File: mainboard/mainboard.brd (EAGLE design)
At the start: 158.8 x 159.4 mm, 60 parts, among them T1 NPN_BC817,215, T2 NPN_BC817,215, T3 NPN_BC817,215

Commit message: Mainboard rev1 wip
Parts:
- removed BOOST_EN: CONNEC_1X01, rhoban:CONNEC_1X01
- removed POWERCAP1, POWERCAP2, SOLENOID1, SOLENOID2: CONNEC_1X02BIG, rhoban:CONNEC_1X02_BIG
- removed R31, R9: 1K, rhoban:R0805
- removed R32, R33, R36: 3K, rhoban:R0805
- removed R34: 2M, rhoban:R0805
- removed R35: 10K, rhoban:R0805
- removed T1, T3, U$15: NPN_BC817,215, rhoban:SOT-23
- removed XT1: CONNEC_ALIM, rhoban:XT60
- added C2: 1uF, SparkFun-Passives:0805@1
- added REG3.3V1: REG_5V, rhoban:TRACOPOWER
- added U$10: DRV5023FAEDBZRQ1, rhoban:SOT-23
- added U$6: 47uF, rhoban:PANASONIC_D
- added U$7, U$8, U$9: (no value), rhoban:PANASONIC_D8
- added X1: JST-XH-06-PIN-LONG-PAD, Rembrandt Electronics - JST XH Connectors v1-0:JST-XH-06-PACKAGE-LONG-PAD
- R1: value 1K -> 10K
- R2, R3: value 3K -> 10K
- U$1, U$11: value TO-247A -> DRV5023FAEDBZRQ1; device to-247_n-channel_igbt:TO-247 -> rhoban:SOT-23
- U$5: value BOOSTER -> DRV5023FAEDBZRQ1; device rhoban:BOOSTER_390V -> rhoban:SOT-23
- moved R7 94.5 mm to (-35.3, -40.5), flipped to the bottom
- moved DRIVER4 90.6 mm to (-11.6, -50.1), turned to 0 degrees
- moved XT60 89.0 mm to (-37.4, 26.2), turned to 180 degrees
- moved U$5 78.3 mm to (14.5, -37.3), flipped to the bottom
- moved U$1 76.3 mm to (39.5, -37.3), flipped to the bottom, turned to 0 degrees
- moved U$11 66.9 mm to (-35.5, -37.3), flipped to the bottom, turned to 0 degrees
- moved DRIVER2 66.0 mm to (31.2, 43.5), turned to 180 degrees
- moved D3 65.0 mm to (3.03, -47.2), turned to 90 degrees
- moved R1 64.6 mm to (39.5, -40.5), flipped to the bottom, turned to 180 degrees
- moved R2 61.7 mm to (14.6, -40.7), flipped to the bottom, turned to 180 degrees
- moved R3 60.1 mm to (-10.4, -40.6), flipped to the bottom, turned to 180 degrees
- moved DRIVER3 59.5 mm to (-44.5, -50.1), turned to 0 degrees
- moved D2 49.6 mm to (-29.7, -47.2), turned to 90 degrees
- moved D1 48.4 mm to (16.6, 40.4), turned to 270 degrees
- moved U$2 41.4 mm to (71.5, -31.8), turned to 90 degrees
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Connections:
- net BAT2 renamed BAT
- removed net BAT1: MAPLE.X8, R7.1, R9.2
- removed net N$1: R1.2, T1.1
- removed net N$17: R31.2, T3.1
- removed net N$2: SOLENOID1.P$2, U$1.P$2
- removed net N$35: R33.1, T3.3, U$11.P$1
- removed net N$36: SOLENOID2.P$2, U$11.P$2
- removed net N$37: BOOST_EN.1, U$15.3
- removed net N$38: R36.1, U$15.1
- removed net N$4: R3.1, T1.3, U$1.P$1
- removed net VBOOST: POWERCAP1.P$2, POWERCAP2.P$2, R34.2, SOLENOID1.P$1, SOLENOID2.P$1, U$5.OUT+
- removed net VMID: D1.2, D2.2, D3.2, D4.2, D5.2, R7.2, XT1.GND, XT60.V+
- new net 12V: C2.2, D1.2, D2.2, D3.2, D4.2, D5.2, REG3.3V1.P$3, U$6.+
- new net HALL1: MAPLE.X14, R1.1, U$1.2
- new net HALL2: MAPLE.X8, R2.1, U$5.2
- new net HALL3: MAPLE.X2, R3.1, U$10.2
- new net HALL4: MAPLE.X31, R7.1, U$11.2
- net 3.3: now also R1.2, R3.2, R7.2, U$1.1, U$10.1, U$11.1, U$5.1, U$7.+, U$8.+, U$9.+; no longer R32.2
- net BOOST_EN: now also X1.3; no longer R36.2
- net CAP: now also X1.6; no longer R34.1, R35.2
- net GND: now also C2.1, REG3.3V1.P$2, U$1.3, U$10.3, U$11.3, U$5.3, U$6.-, U$7.-, U$8.-, U$9.-, X1.1; no longer POWERCAP1.P$1, POWERCAP2.P$1, R35.1, R9.1, T1.2, T3.2, U$1.P$3, U$11.P$3, U$15.2, U$5.IN-, U$5.OUT-
- net KICK1: now also X1.4; no longer R1.1, R2.1
- net KICK2: now also X1.5; no longer R31.1, R32.1
- net VIN: now also REG3.3V1.P$1, X1.2, XT60.V+; no longer R3.2, R33.2, U$5.VIN, XT1.V+
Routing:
- net GND: track 89.1 -> 0.00 mm
- net VBOOST: track 26.0 -> 0.00 mm
- net N$2: track 13.5 -> 0.00 mm
- net N$36: track 11.6 -> 0.00 mm
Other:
- board size 158.8 x 159.4 mm -> 158.8 x 136.4 mm
- board text added: "12V"
- board text added: "3.3V"
- board text added: "5V"
- board text added: "RHOBAN SSL rev1"
- board text removed: "BOOST_EN"
- board text removed: "REV0"
- board text removed: "RHOBAN SSL MAINBOARD"
- board text removed: "RHOBAN SSL rev0"

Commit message: Updating designs
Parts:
- moved D1 1.24 mm to (15.4, 40.7)
- moved D5 1.20 mm to (36.5, -47.1)
- moved D4 1.17 mm to (-17.0, 40.7)
- moved D3 1.10 mm to (4.13, -47.2)
- moved D2 0.91 mm to (-28.8, -47.3)
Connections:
- net DRIVERS_CS2: now also MAPLE.X1; no longer MAPLE.X26
- net IRQ3: now also MAPLE.X0; no longer MAPLE.X25
- net KICK1: now also MAPLE.X25; no longer MAPLE.X0
- net KICK2: now also MAPLE.X26; no longer MAPLE.X1
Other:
- board text added: "DRIVER"
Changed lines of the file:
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@@
 <dimension x1="-59.75" y1="43.75" x2="-59.75" y2="-38.25" x3="-107.75" y3="2.75" layer="51"/>
 <dimension x1="1.7" y1="60.8" x2="2" y2="-77.5" x3="113.45066875" y3="-8.107915625" layer="51"/>
-<text x="38.75" y="-9.5" size="10" layer="112" rot="R180">1</text>
-<text x="8" y="-8.75" size="10" layer="112" rot="R180">2</text>
-<text x="-12.25" y="13.25" size="10" layer="112" rot="R180">5</text>
-<text x="-25" y="-8.5" size="10" layer="112" rot="R180">3</text>
-<text x="19.5" y="12.75" size="10" layer="112" rot="R180">4</text>
+<text x="37.25" y="-21.7" size="10" layer="112" rot="R180">1</text>
+<text x="6.5" y="-21.85" size="10" layer="112" rot="R180">2</text>
+<text x="-12.25" y="24.65" size="10" layer="112" rot="R180">5</text>
+<text x="-26.2" y="-21.2" size="10" layer="112" rot="R180">3</text>
+<text x="19.5" y="24.15" size="10" layer="112" rot="R180">4</text>
 <text x="-55.25" y="-14" size="1.778" layer="121">3.3V</text>
 <text x="-54.5" y="-23.5" size="1.778" layer="121">5V</text>
@@
 <wire x1="12.431" y1="-66.38" x2="12.744" y2="-66.525" width="0" layer="20"/>
 <wire x1="12.744" y1="-66.525" x2="13.029" y2="-66.725" width="0" layer="20"/>
+<text x="38.7" y="-34" size="3" layer="122">1</text>
+<text x="13.3" y="-34.5" size="3" layer="122">2</text>
+<text x="-11.6" y="-34.2" size="3" layer="122">3</text>
+<text x="-36.7" y="-34.5" size="3" layer="122">4</text>
+<text x="-38.5" y="-20.6" size="3" layer="121">DRIVER</text>
+<text x="-5.4" y="-20.8" size="3" layer="121">DRIVER</text>
+<text x="25.6" y="-20.9" size="3" layer="121">DRIVER</text>
+<text x="8.4" y="24.8" size="3" layer="121">DRIVER</text>
+<text x="-23.9" y="25" size="3" layer="121">DRIVER</text>
 </plain>
 <attributes>
@@
 <attribute name="FARNELL" value="1593459,1593459,1593463" x="-1.285" y="43.515" size="1.778" layer="27" rot="R180" display="off"/>
 </element>
-<element name="D5" library="SparkFun-DiscreteSemi" package="SOD-323" value="" x="35.265" y="-47.11" rot="R90">
-<attribute name="FARNELL" value="8737843RL" x="31.455" y="-50.92" size="1.778" layer="27" rot="R90" display="off"/>
-</element>
-<element name="D1" library="SparkFun-DiscreteSemi" package="SOD-323" value="" x="16.62" y="40.36" rot="R270">
-<attribute name="FARNELL" value="8737843RL" x="16.62" y="40.36" size="1.778" layer="27" rot="R270" display="off"/>
-</element>
-<element name="D2" library="SparkFun-DiscreteSemi" package="SOD-323" value="" x="-29.67" y="-47.155" rot="R90">
-<attribute name="FARNELL" value="8737843RL" x="-29.67" y="-47.155" size="1.778" layer="27" rot="R90" display="off"/>
-</element>
-<element name="D3" library="SparkFun-DiscreteSemi" package="SOD-323" value="" x="3.03" y="-47.155" rot="R90">
-<attribute name="FARNELL" value="8737843RL" x="3.03" y="-47.155" size="1.778" layer="27" rot="R90" display="off"/>
-</element>
-<element name="D4" library="SparkFun-DiscreteSemi" package="SOD-323" value="" x="-15.89" y="40.34" rot="R270">
-<attribute name="FARNELL" value="8737843RL" x="-15.89" y="40.34" size="1.778" layer="27" rot="R270" display="off"/>
+<element name="D5" library="SparkFun-DiscreteSemi" package="SOD-323" value="" x="36.465" y="-47.11" rot="R90">
+<attribute name="FARNELL" value="8737843RL" x="32.655" y="-50.92" size="1.778" layer="27" rot="R90" display="off"/>
+</element>
+<element name="D1" library="SparkFun-DiscreteSemi" package="SOD-323" value="" x="15.42" y="40.66" rot="R270">
+<attribute name="FARNELL" value="8737843RL" x="15.42" y="40.66" size="1.778" layer="27" rot="R270" display="off"/>
+</element>
+<element name="D2" library="SparkFun-DiscreteSemi" package="SOD-323" value="" x="-28.77" y="-47.255" rot="R90">
+<attribute name="FARNELL" value="8737843RL" x="-28.77" y="-47.255" size="1.778" layer="27" rot="R90" display="off"/>
+</element>
+<element name="D3" library="SparkFun-DiscreteSemi" package="SOD-323" value="" x="4.13" y="-47.155" rot="R90">
+<attribute name="FARNELL" value="8737843RL" x="4.13" y="-47.155" size="1.778" layer="27" rot="R90" display="off"/>
+</element>
+<element name="D4" library="SparkFun-DiscreteSemi" package="SOD-323" value="" x="-16.99" y="40.74" rot="R270">
+<attribute name="FARNELL" value="8737843RL" x="-16.99" y="40.74" size="1.778" layer="27" rot="R270" display="off"/>
 </element>
 <element name="R10" library="rhoban" package="R0805" value="10K" x="34.635" y="32.3" rot="R180">
@@
 <signals>
 <signal name="KICK2">
-<contactref element="MAPLE" pad="X1"/>
 <contactref element="X1" pad="5"/>
-<wire x1="-1.56" y1="55.25" x2="57.37" y2="10.2" width="0" layer="19" extent="1-1"/>
+<contactref element="MAPLE" pad="X26"/>
+<wire x1="-1.56" y1="55.25" x2="42.13" y2="17.82" width="0" layer="19" extent="1-1"/>
 </signal>
 <signal name="3.3" class="1">
@@
 </signal>
 <signal name="IRQ3">
-<contactref element="MAPLE" pad="X25"/>
 <contactref element="COM3" pad="IRQ"/>
-<wire x1="6.985" y1="-60.325" x2="42.13" y2="20.36" width="0" layer="19" extent="1-1"/>
+<contactref element="MAPLE" pad="X0"/>
+<wire x1="6.985" y1="-60.325" x2="57.37" y2="7.66" width="0" layer="19" extent="1-1"/>
 </signal>
 <signal name="IRQ2">
@@
 </signal>
 <signal name="KICK1">
-<contactref element="MAPLE" pad="X0"/>
 <contactref element="X1" pad="4"/>
-<wire x1="0.98" y1="55.25" x2="57.37" y2="7.66" width="0" layer="19" extent="1-1"/>
+<contactref element="MAPLE" pad="X25"/>
+<wire x1="0.98" y1="55.25" x2="42.13" y2="20.36" width="0" layer="19" extent="1-1"/>
 </signal>
 <signal name="BOOST_EN">
@@
 </signal>
 <signal name="DRIVERS_CS2">
-<contactref element="MAPLE" pad="X26"/>
 <contactref element="DRIVER2" pad="CS"/>
-<wire x1="42.13" y1="17.82" x2="19.0578" y2="44.0478" width="0" layer="19" extent="1-1"/>
+<contactref element="MAPLE" pad="X1"/>
+<wire x1="19.0578" y1="44.0478" x2="57.37" y2="10.2" width="0" layer="19" extent="1-1"/>
 </signal>
 <signal name="DRIVERS_CS1">
@@
 <contactref element="DRIVER1" pad="VDRIVER"/>
 <contactref element="D5" pad="1"/>
-<wire x1="35.265" y1="-48.26" x2="35.3672" y2="-50.7978" width="0" layer="19" extent="1-1"/>
+<wire x1="36.465" y1="-48.26" x2="35.3672" y2="-50.7978" width="0" layer="19" extent="1-1"/>
 </signal>
 <signal name="N$9">
 <contactref element="DRIVER4" pad="VDRIVER"/>
 <contactref element="D3" pad="1"/>
-<wire x1="3.03" y1="-48.305" x2="3.1322" y2="-50.5928" width="0" layer="19" extent="1-1"/>
+<wire x1="4.13" y1="-48.305" x2="3.1322" y2="-50.5928" width="0" layer="19" extent="1-1"/>
 </signal>
 <signal name="N$10">
 <contactref element="DRIVER5" pad="VDRIVER"/>
 <contactref element="D4" pad="1"/>
-<wire x1="-15.89" y1="41.49" x2="-15.9922" y2="44.0278" width="0" layer="19" extent="1-1"/>
+<wire x1="-16.99" y1="41.89" x2="-15.9922" y2="44.0278" width="0" layer="19" extent="1-1"/>
 </signal>
 <signal name="N$12">
 <contactref element="DRIVER3" pad="VDRIVER"/>
 <contactref element="D2" pad="1"/>
-<wire x1="-29.67" y1="-48.305" x2="-29.8178" y2="-50.5928" width="0" layer="19" extent="1-1"/>
+<wire x1="-28.77" y1="-48.405" x2="-29.8178" y2="-50.5928" width="0" layer="19" extent="1-1"/>
 </signal>
 <signal name="N$13">
 <contactref element="DRIVER2" pad="VDRIVER"/>
 <contactref element="D1" pad="1"/>
-<wire x1="16.62" y1="41.51" x2="16.5178" y2="44.0478" width="0" layer="19" extent="1-1"/>
+<wire x1="15.42" y1="41.81" x2="16.5178" y2="44.0478" width="0" layer="19" extent="1-1"/>
 </signal>
 <signal name="COM_CE">
@@
 <wire x1="-61.35" y1="-27.5" x2="-69.25" y2="-24.1" width="0" layer="19" extent="1-1"/>
 <wire x1="-55.33" y1="-27.75" x2="-61.35" y2="-27.5" width="0" layer="19" extent="1-1"/>
-<wire x1="-29.67" y1="-46.005" x2="-55.33" y2="-27.75" width="0" layer="19" extent="1-1"/>
-<wire x1="3.03" y1="-46.005" x2="-29.67" y2="-46.005" width="0" layer="19" extent="1-1"/>
-<wire x1="35.265" y1="-45.96" x2="3.03" y2="-46.005" width="0" layer="19" extent="1-1"/>
-<wire x1="-15.89" y1="39.19" x2="-55.33" y2="-27.75" width="0" layer="19" extent="1-1"/>
-<wire x1="16.62" y1="39.21" x2="-15.89" y2="39.19" width="0" layer="19" extent="1-1"/>
+<wire x1="-28.77" y1="-46.105" x2="-55.33" y2="-27.75" width="0" layer="19" extent="1-1"/>
+<wire x1="4.13" y1="-46.005" x2="-28.77" y2="-46.105" width="0" layer="19" extent="1-1"/>
+<wire x1="36.465" y1="-45.96" x2="4.13" y2="-46.005" width="0" layer="19" extent="1-1"/>
+<wire x1="-16.99" y1="39.59" x2="-55.33" y2="-27.75" width="0" layer="19" extent="1-1"/>
+<wire x1="15.42" y1="39.51" x2="-16.99" y2="39.59" width="0" layer="19" extent="1-1"/>
 </signal>
 <signal name="BAT">

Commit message: mainboard updates
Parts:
- added U$15: SRB22A2FBBNN, rhoban:SRB22A2FBBNN
- moved R11 110.5 mm to (-50.5, -40.7)
- moved R10 110.3 mm to (-50.5, -37.9)
- moved RECEIVE 21.2 mm to (-26.5, 56.1)
- moved R6 21.2 mm to (-25.9, 52.3)
- moved U$8 9.24 mm to (65.6, -10.1), turned to 0 degrees
- moved U$9 8.10 mm to (-10.1, -60.9), turned to 270 degrees
- moved XT60 5.89 mm to (-38.4, 20.4)
- moved U$7 5.32 mm to (-63.0, 17.3), turned to 180 degrees
- moved C2 1.02 mm to (-69.0, -24.0)
- moved R8 0.71 mm to (63.4, 32.8), turned to 180 degrees
- moved C7 0.60 mm to (-69.4, -9.59)
- moved C1 0.32 mm to (-69.2, -16.7)
- moved U$13 0.25 mm to (68.8, 22.9), turned to 270 degrees
- moved D1 0.14 mm to (15.5, 40.6)
- moved DRIVER2 0.08 mm to (31.3, 43.5)
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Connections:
- new net VIN_BAT: U$15.P$2, XT60.V+
- net VIN: now also U$15.P$1; no longer XT60.V+
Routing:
- net VIN: track 0.00 -> 172.7 mm
- net GND: track 0.00 -> 161.0 mm
- net VIN_BAT: track 0.00 -> 19.4 mm
- net 3.3: track 0.00 -> 4.44 mm, vias 0 -> 1
- net N$7: track 0.00 -> 4.40 mm, vias 0 -> 1
- net N$13: track 0.00 -> 2.75 mm
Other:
- board text added: "COM1"
- board text added: "COM2"
- board text added: "COM3"
- board text added: "IR EMIT"
- board text added: "IR RCV"
- board text added: "KICKER"
- board text added: "MAIN"
- board text added: "SWITCH"

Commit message: farnell attrs
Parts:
- moved U$12 78.9 mm to (-7.55, 54.8), turned to 0 degrees
- moved U$13 74.5 mm to (0.86, 53.5), turned to 0 degrees
- moved X1 74.2 mm to (68.1, 21.1), turned to 90 degrees
- moved R8 73.4 mm to (-7.64, 51.2), turned to 0 degrees
- moved EMIT 40.3 mm to (66.8, 37.6)
- moved R4 40.3 mm to (72.3, 32.1)
- moved R5 40.3 mm to (72.5, 35.7)
- moved T2 40.3 mm to (67.5, 33.1)
- moved R6 39.3 mm to (-60.0, 32.7)
- moved RECEIVE 39.3 mm to (-60.6, 36.5)
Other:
- outline, holes or cut-outs redrawn

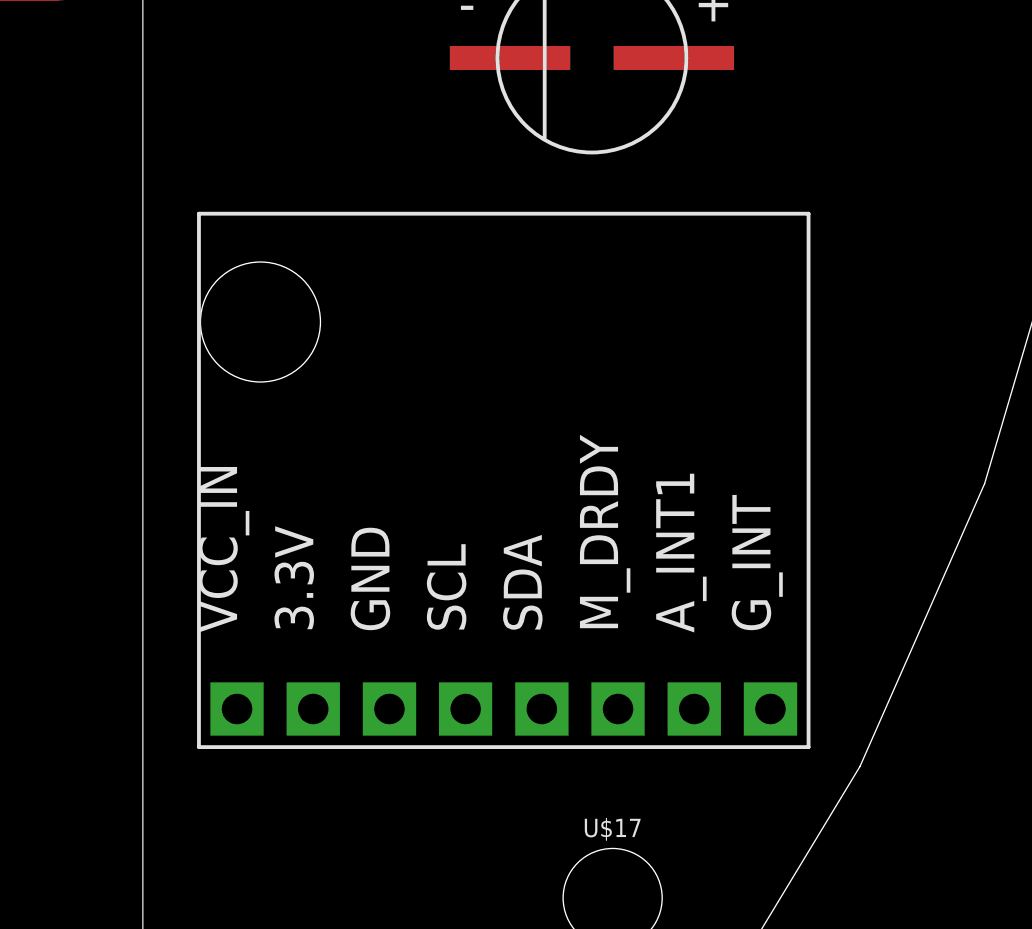
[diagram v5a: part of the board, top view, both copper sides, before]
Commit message: Minor placement changes
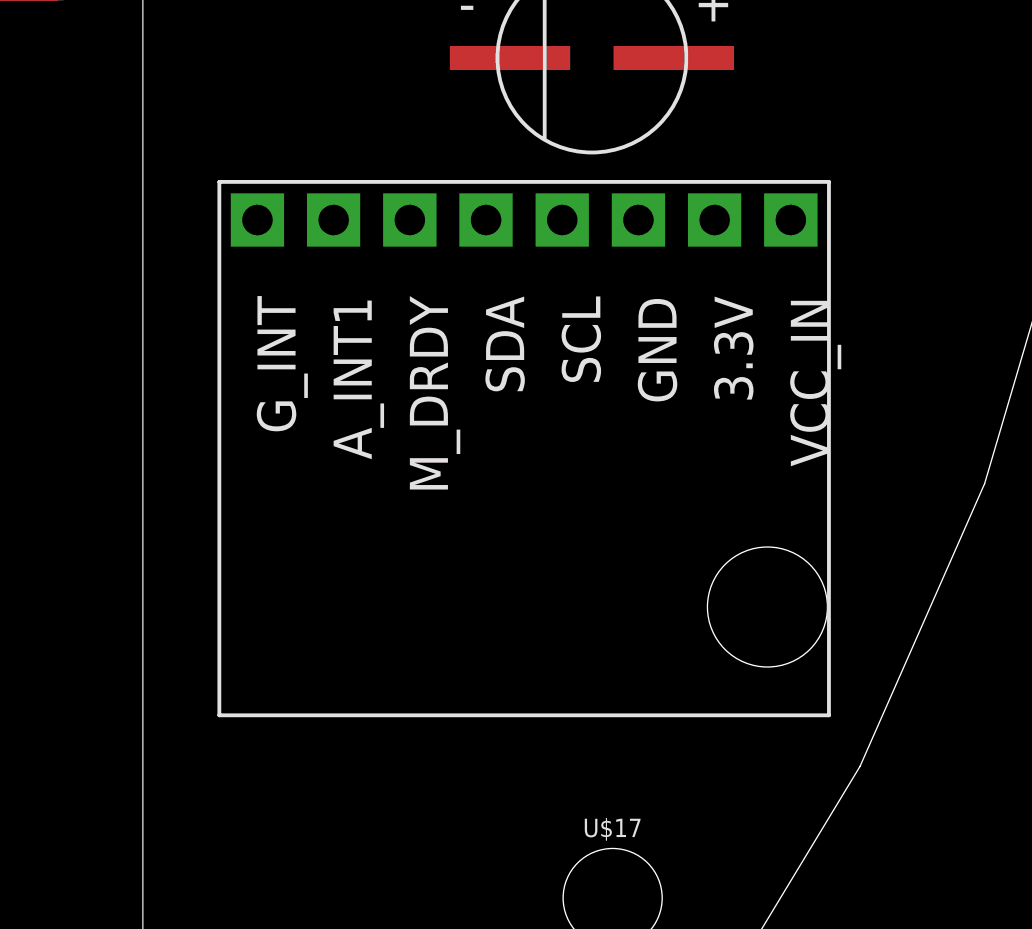
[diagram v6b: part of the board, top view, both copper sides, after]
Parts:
- moved U$2 23.6 mm to (54.4, -15.5), turned to 270 degrees

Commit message: Updating BOMs and ATTRs
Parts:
- U$7, U$8, U$9: value (none) -> 220uF
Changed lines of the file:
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@@
 <attribute name="FARNELL" value="2496946" x="-65.8" y="-36.25" size="1.778" layer="27" rot="R90" display="off"/>
 </element>
-<element name="U$7" library="rhoban" package="PANASONIC_D8" value="" x="-62.950071875" y="17.25001875" rot="R180"/>
-<element name="X1" library="Rembrandt Electronics - JST XH Connectors v1-0" package="JST-XH-06-PACKAGE-LONG-PAD" value="JST-XH-06-PIN-LONG-PAD" x="68.149975" y="21.149953125" rot="R90"/>
-<element name="U$8" library="rhoban" package="PANASONIC_D8" value="" x="65.550075" y="-10.1000125"/>
-<element name="U$9" library="rhoban" package="PANASONIC_D8" value="" x="-10.1000125" y="-60.900071875" rot="R270"/>
+<element name="U$7" library="rhoban" package="PANASONIC_D8" value="220uF" x="-62.950071875" y="17.25001875" rot="R180">
+<attribute name="FARNELL" value="1850103" x="-62.950071875" y="17.25001875" size="1.778" layer="27" rot="R180" display="off"/>
+</element>
+<element name="X1" library="Rembrandt Electronics - JST XH Connectors v1-0" package="JST-XH-06-PACKAGE-LONG-PAD" value="JST-XH-06-PIN-LONG-PAD" x="68.149975" y="21.149953125" rot="R90">
+<attribute name="FARNELL" value="-" x="68.149975" y="21.149953125" size="1.778" layer="27" rot="R90" display="off"/>
+</element>
+<element name="U$8" library="rhoban" package="PANASONIC_D8" value="220uF" x="65.550075" y="-10.1000125">
+<attribute name="FARNELL" value="1850103" x="65.550075" y="-10.1000125" size="1.778" layer="27" display="off"/>
+</element>
+<element name="U$9" library="rhoban" package="PANASONIC_D8" value="220uF" x="-10.1000125" y="-60.900071875" rot="R270">
+<attribute name="FARNELL" value="1850103" x="-10.1000125" y="-60.900071875" size="1.778" layer="27" rot="R270" display="off"/>
+</element>
 <element name="U$1" library="rhoban" package="SOT-23" value="DRV5023FAEDBZRQ1" x="39.5" y="-37.3" rot="MR0">
 <attribute name="FARNELL" value="2673327RL" x="39.5" y="-37.3" size="1.778" layer="28" rot="MR0" display="off"/>
